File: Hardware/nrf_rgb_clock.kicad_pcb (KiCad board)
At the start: 4 copper layers, 230 x 230 mm, 216 parts, among them J1 Conn_01x02, J3 Conn_01x07_Pin, U2 MP4562, Y1 32MHz

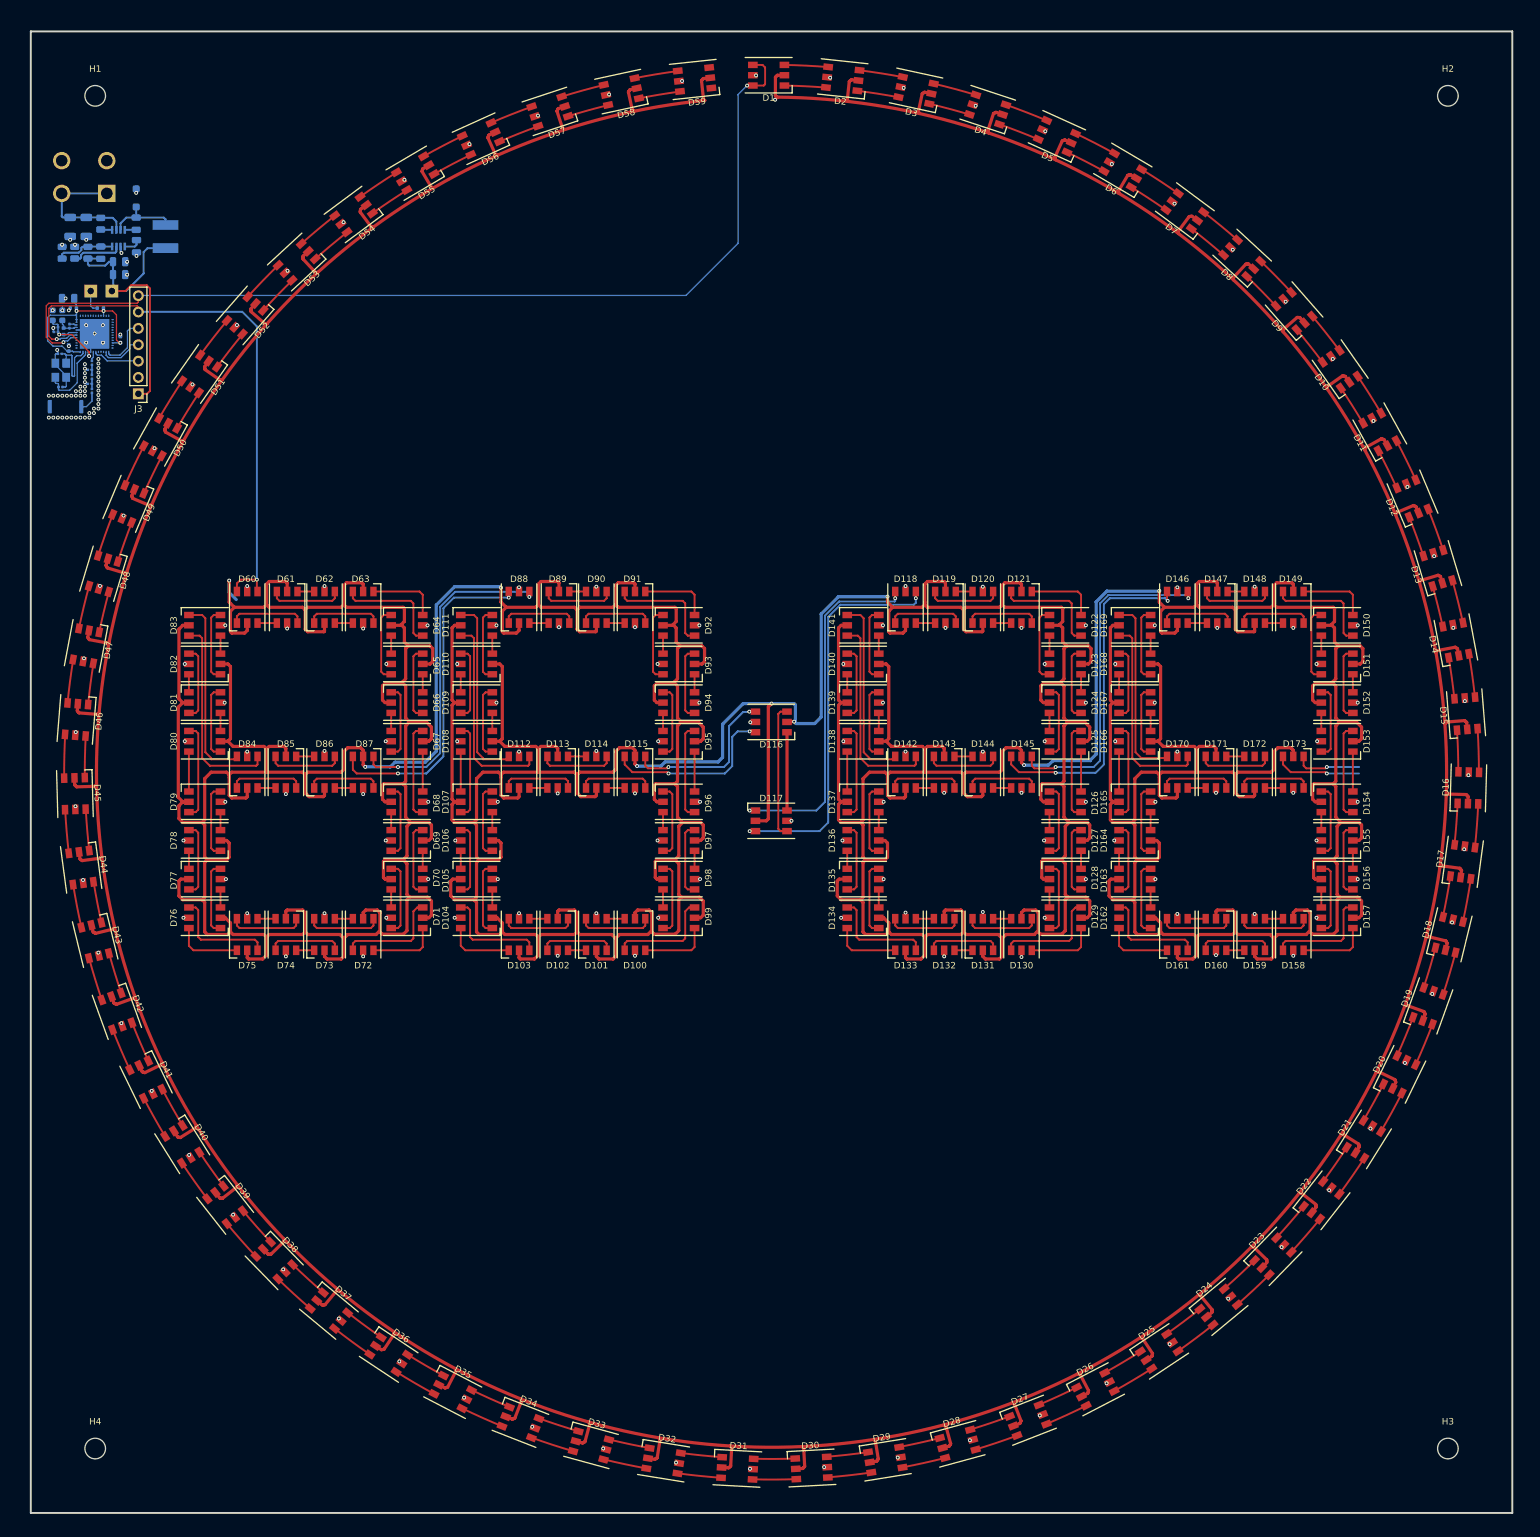
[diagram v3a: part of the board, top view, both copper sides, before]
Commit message: finalized layout, everything on top + LCSC numbers
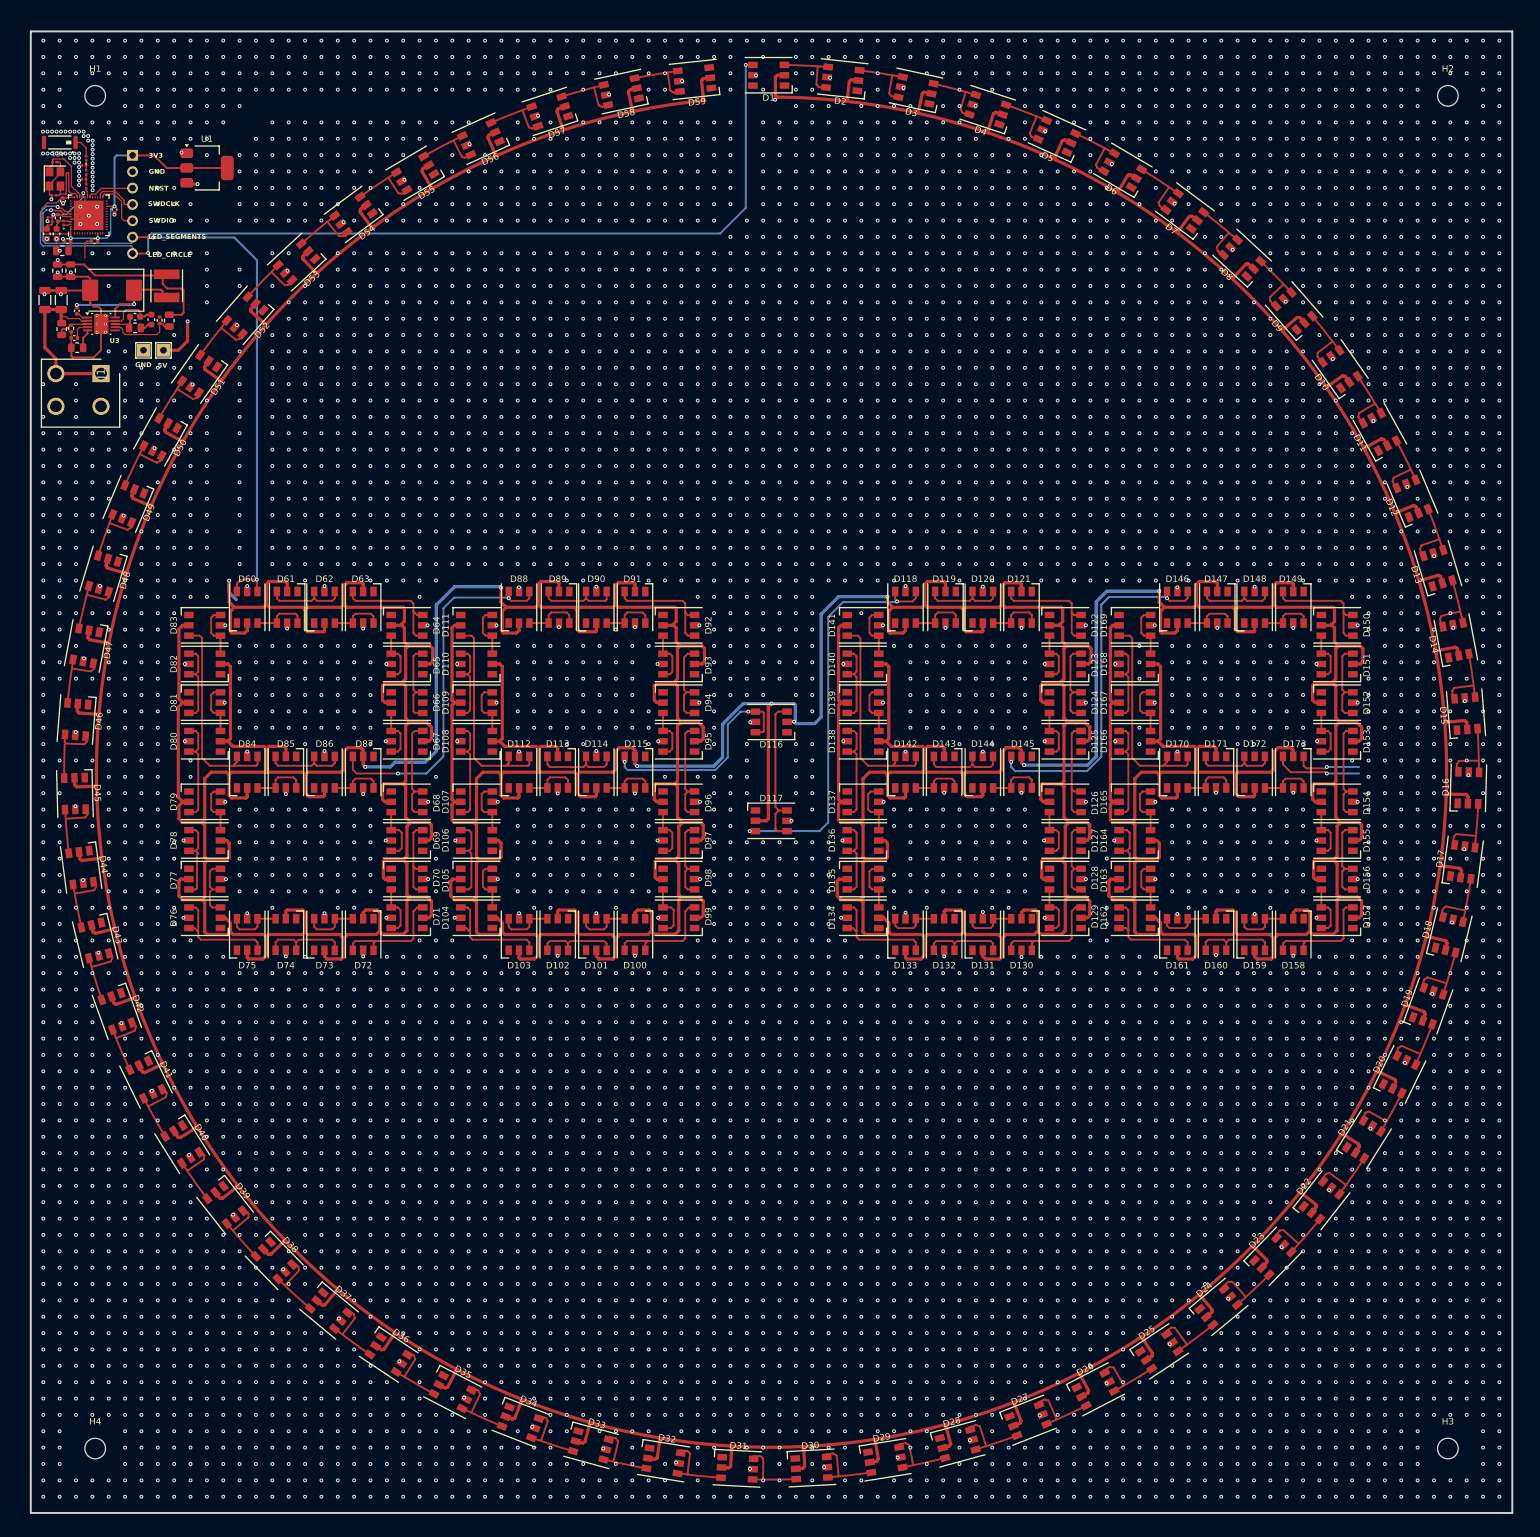
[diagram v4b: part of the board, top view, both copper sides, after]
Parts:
- removed 3V3, GND: TestPoint, TestPoint:TestPoint_THTPad_2.0x2.0mm_Drill1.0mm
- removed C10, C11: 4u7 100VDC, Capacitor_SMD:C_1206_3216Metric
- removed C12: 100n 100VDC, Capacitor_SMD:C_0805_2012Metric
- removed C13, C14: 22u 6.3V, Capacitor_SMD:C_0805_2012Metric
- removed C15: 15p, Capacitor_SMD:C_0805_2012Metric
- removed C16: 22n, Capacitor_SMD:C_0805_2012Metric
- removed D174: ACDBMS2100-HF, Diode_SMD:D_SOD-123F
- removed L5: 10u, ProjectFootprints:NRS5040T3R3NMGJV
- removed R1: 0R, Resistor_SMD:R_0805_2012Metric
- removed R2: 210k, Resistor_SMD:R_0805_2012Metric
- removed R3: 68k, Resistor_SMD:R_0805_2012Metric
- removed R4: 47k, Resistor_SMD:R_0805_2012Metric
- removed U2: MP4562, ProjectFootprints:MP4562
- added C21: 100n, Capacitor_SMD:C_0402_1005Metric, F.Cu at (232.2, 148.6)
- added C22: 47u 6.3V, Capacitor_SMD:C_0805_2012Metric, F.Cu at (229.2, 142.3)
- added C23: 47u 6.3V, Capacitor_SMD:C_0805_2012Metric, F.Cu at (231.2, 142.3)
- added C24: 4u7 100VDC, Capacitor_SMD:C_1206_3216Metric, F.Cu at (227.2, 146.9)
- added C25: 4u7 100VDC, Capacitor_SMD:C_1206_3216Metric, F.Cu at (229.7, 146.9)
- added C26: 10n, Capacitor_SMD:C_0402_1005Metric, F.Cu at (231.8, 152.8)
- added C27: ~, Capacitor_SMD:C_0603_1608Metric, F.Cu at (241.2, 149.5)
- added C28: 4n7, Capacitor_SMD:C_0603_1608Metric, F.Cu at (243.7, 149.9)
- added D175: B360, Diode_SMD:D_SMC, F.Cu at (237.6, 145.4)
- added L6: 10u, ProjectFootprints:NRS5040T3R3NMGJV, F.Cu at (246.1, 144.7)
- added R10: 20k, Resistor_SMD:R_0805_2012Metric, F.Cu at (241.2, 151.2)
- added R11: 27k, Resistor_SMD:R_0805_2012Metric, F.Cu at (246.5, 150.1)
- added R12: 5.1k, Resistor_SMD:R_0402_1005Metric, F.Cu at (245.0, 150.1)
- added R5: 110k, Resistor_SMD:R_0805_2012Metric, F.Cu at (229.8, 151.4)
- added R7: 10k, Resistor_SMD:R_0402_1005Metric, F.Cu at (231.3, 151.3)
- added R9: 412k, Resistor_SMD:R_0805_2012Metric, F.Cu at (232.2, 154.3)
- added TP3: TestPoint, TestPoint:TestPoint_THTPad_2.0x2.0mm_Drill1.0mm, F.Cu at (245.6, 154.7)
- added TP4: TestPoint, TestPoint:TestPoint_THTPad_2.0x2.0mm_Drill1.0mm, F.Cu at (242.5, 154.7)
- added U1: AMS1117-3.3, Package_TO_SOT_SMD:SOT-223-3_TabPin2, F.Cu at (252.3, 126.4)
- added U3: TPS54260DGQ, Package_SO:MSOP-10-1EP_3x3mm_P0.5mm_EP2.2x3.1mm_Mask1.83x1.89mm_ThermalVias, F.Cu at (236.0, 150.6)
- AE1, C1, C17, C18, C19, C2, C20, C3, C4, C5, C6, C7, C8, C9, FB1, J1, L1, L2, L3, L4, U4, Y1: moved to F.Cu
- J3: moved to B.Cu
- moved AE1 41.0 mm to (229.5, 122.4)
- moved J3 37.0 mm to (240.8, 124.4)
- moved L2 36.1 mm to (233.6, 124.9), turned to 90 degrees
- moved C17 34.9 mm to (228.7, 125.5)
- moved C8 33.9 mm to (233.2, 126.0)
- moved L3 31.7 mm to (233.6, 127.1), turned to 90 degrees
- moved Y1 29.7 mm to (228.8, 128.1), turned to -90 degrees
- moved C9 29.6 mm to (233.2, 128.2)
- moved J1 28.0 mm to (235.9, 158.3), turned to -90 degrees
- moved L4 27.4 mm to (233.6, 129.2), turned to 90 degrees
- moved C18 24.6 mm to (228.6, 130.7)
- moved C20 22.8 mm to (230.0, 131.6), turned to 90 degrees
- moved C19 20.2 mm to (238.0, 132.8), turned to 90 degrees
- moved U4 18.4 mm to (234.0, 133.8), turned to 90 degrees
- moved C6 17.8 mm to (228.0, 134.1)
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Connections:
- C1 pad 2: VDD_NRF -> +3V3
- C19 pad 2: VDD_NRF -> +3V3
- C2 pad 2: VDD_NRF -> +3V3
- C20 pad 2: VDD_NRF -> +3V3
- C3 pad 2: VDD_NRF -> +3V3
- D1 pad 1: Net-(D1-BO) -> unconnected-(D1-VCC-Pad1)
- D1 pad 6: LED_CIRCLE -> unconnected-(D1-BI-Pad6)
- D10 pad 1: Net-(D10-BO) -> unconnected-(D10-VCC-Pad1)
- D10 pad 4: Net-(D10-DI) -> Net-(D10-BI)
- D100 pad 1: Net-(D100-BO) -> unconnected-(D100-VCC-Pad1)
- D100 pad 4: Net-(D100-DI) -> Net-(D100-BI)
- D101 pad 1: Net-(D101-BO) -> unconnected-(D101-VCC-Pad1)
- D101 pad 6: Net-(D100-BO) -> Net-(D100-DO)
- D102 pad 1: Net-(D102-BO) -> unconnected-(D102-VCC-Pad1)
- D102 pad 6: Net-(D101-BO) -> Net-(D101-DO)
- D103 pad 1: Net-(D103-BO) -> unconnected-(D103-VCC-Pad1)
- D103 pad 6: Net-(D102-BO) -> Net-(D102-DO)
- D104 pad 1: Net-(D104-BO) -> unconnected-(D104-VCC-Pad1)
- D104 pad 6: Net-(D103-BO) -> Net-(D103-DO)
- D105 pad 1: Net-(D105-BO) -> unconnected-(D105-VCC-Pad1)
- D105 pad 6: Net-(D104-BO) -> Net-(D104-DO)
- D106 pad 1: Net-(D106-BO) -> unconnected-(D106-VCC-Pad1)
- D106 pad 6: Net-(D105-BO) -> Net-(D105-DO)
- D107 pad 1: Net-(D107-BO) -> unconnected-(D107-VCC-Pad1)
- D107 pad 6: Net-(D106-BO) -> Net-(D106-DO)
- D108 pad 1: Net-(D108-BO) -> unconnected-(D108-VCC-Pad1)
- D108 pad 6: Net-(D107-BO) -> Net-(D107-DO)
- D109 pad 1: Net-(D109-BO) -> unconnected-(D109-VCC-Pad1)
- D109 pad 6: Net-(D108-BO) -> Net-(D108-DO)
- D11 pad 1: Net-(D11-BO) -> unconnected-(D11-VCC-Pad1)
- D11 pad 6: Net-(D10-BO) -> Net-(D10-DO)
- D110 pad 1: Net-(D110-BO) -> unconnected-(D110-VCC-Pad1)
- D110 pad 6: Net-(D109-BO) -> Net-(D109-DO)
- D111 pad 1: Net-(D111-BO) -> unconnected-(D111-VCC-Pad1)
- D111 pad 6: Net-(D110-BO) -> Net-(D110-DO)
- D112 pad 1: Net-(D112-BO) -> unconnected-(D112-VCC-Pad1)
- D112 pad 6: Net-(D111-BO) -> Net-(D111-DO)
- D113 pad 1: Net-(D113-BO) -> unconnected-(D113-VCC-Pad1)
- D113 pad 6: Net-(D112-BO) -> Net-(D112-DO)
- D114 pad 1: Net-(D114-BO) -> unconnected-(D114-VCC-Pad1)
- D114 pad 6: Net-(D113-BO) -> Net-(D113-DO)
- D115 pad 1: /led_segment1/LED_BO -> unconnected-(D115-VCC-Pad1)
- D115 pad 6: Net-(D114-BO) -> Net-(D114-DO)
- D116 pad 1: Net-(D116-BO) -> unconnected-(D116-VCC-Pad1)
- D116 pad 4: /led_segment1/LED_BO -> /led_segment1/LED_DO
- D117 pad 1: /led_segment2/LED_BI -> unconnected-(D117-VCC-Pad1)
- D117 pad 6: Net-(D116-BO) -> Net-(D116-DO)
- D118 pad 1: Net-(D118-BO) -> unconnected-(D118-VCC-Pad1)
- D118 pad 6: /led_segment2/LED_BI -> /led_segment2/LED_DI
- D119 pad 1: Net-(D119-BO) -> unconnected-(D119-VCC-Pad1)
- D119 pad 6: Net-(D118-BO) -> Net-(D118-DO)
- D12 pad 1: Net-(D12-BO) -> unconnected-(D12-VCC-Pad1)
- D12 pad 6: Net-(D11-BO) -> Net-(D11-DO)
- D120 pad 1: Net-(D120-BO) -> unconnected-(D120-VCC-Pad1)
- D120 pad 6: Net-(D119-BO) -> Net-(D119-DO)
- D121 pad 1: Net-(D121-BO) -> unconnected-(D121-VCC-Pad1)
- D121 pad 6: Net-(D120-BO) -> Net-(D120-DO)
- D122 pad 1: Net-(D122-BO) -> unconnected-(D122-VCC-Pad1)
- D122 pad 6: Net-(D121-BO) -> Net-(D121-DO)
- D123 pad 1: Net-(D123-BO) -> unconnected-(D123-VCC-Pad1)
- D123 pad 6: Net-(D122-BO) -> Net-(D122-DO)
- D124 pad 1: Net-(D124-BO) -> unconnected-(D124-VCC-Pad1)
- D124 pad 6: Net-(D123-BO) -> Net-(D123-DO)
- D125 pad 1: Net-(D125-BO) -> unconnected-(D125-VCC-Pad1)
- D125 pad 6: Net-(D124-BO) -> Net-(D124-DO)
- D126 pad 1: Net-(D126-BO) -> unconnected-(D126-VCC-Pad1)
- D126 pad 6: Net-(D125-BO) -> Net-(D125-DO)
- D127 pad 1: Net-(D127-BO) -> unconnected-(D127-VCC-Pad1)
- D127 pad 6: Net-(D126-BO) -> Net-(D126-DO)
- D128 pad 1: Net-(D128-BO) -> unconnected-(D128-VCC-Pad1)
- D128 pad 6: Net-(D127-BO) -> Net-(D127-DO)
- D129 pad 1: Net-(D129-BO) -> unconnected-(D129-VCC-Pad1)
- D129 pad 6: Net-(D128-BO) -> Net-(D128-DO)
- D13 pad 1: Net-(D13-BO) -> unconnected-(D13-VCC-Pad1)
- D13 pad 6: Net-(D12-BO) -> Net-(D12-DO)
- D130 pad 1: Net-(D130-BO) -> unconnected-(D130-VCC-Pad1)
- D130 pad 6: Net-(D129-BO) -> Net-(D129-DO)
- D131 pad 1: Net-(D131-BO) -> unconnected-(D131-VCC-Pad1)
- D131 pad 6: Net-(D130-BO) -> Net-(D130-DO)
- D132 pad 1: Net-(D132-BO) -> unconnected-(D132-VCC-Pad1)
- D132 pad 6: Net-(D131-BO) -> Net-(D131-DO)
- D133 pad 1: Net-(D133-BO) -> unconnected-(D133-VCC-Pad1)
- D133 pad 6: Net-(D132-BO) -> Net-(D132-DO)
- D134 pad 1: Net-(D134-BO) -> unconnected-(D134-VCC-Pad1)
- D134 pad 6: Net-(D133-BO) -> Net-(D133-DO)
- D135 pad 1: Net-(D135-BO) -> unconnected-(D135-VCC-Pad1)
- D135 pad 6: Net-(D134-BO) -> Net-(D134-DO)
- D136 pad 1: Net-(D136-BO) -> unconnected-(D136-VCC-Pad1)
- D136 pad 6: Net-(D135-BO) -> Net-(D135-DO)
- D137 pad 1: Net-(D137-BO) -> unconnected-(D137-VCC-Pad1)
- D137 pad 6: Net-(D136-BO) -> Net-(D136-DO)
- D138 pad 1: Net-(D138-BO) -> unconnected-(D138-VCC-Pad1)
- D138 pad 6: Net-(D137-BO) -> Net-(D137-DO)
- D139 pad 1: Net-(D139-BO) -> unconnected-(D139-VCC-Pad1)
- D139 pad 6: Net-(D138-BO) -> Net-(D138-DO)
- D14 pad 1: Net-(D14-BO) -> unconnected-(D14-VCC-Pad1)
- D14 pad 6: Net-(D13-BO) -> Net-(D13-DO)
- D140 pad 1: Net-(D140-BO) -> unconnected-(D140-VCC-Pad1)
- D140 pad 6: Net-(D139-BO) -> Net-(D139-DO)
- D141 pad 1: Net-(D141-BO) -> unconnected-(D141-VCC-Pad1)
- D141 pad 6: Net-(D140-BO) -> Net-(D140-DO)
- D142 pad 1: Net-(D142-BO) -> unconnected-(D142-VCC-Pad1)
- D142 pad 6: Net-(D141-BO) -> Net-(D141-DO)
- D143 pad 1: Net-(D143-BO) -> unconnected-(D143-VCC-Pad1)
- D143 pad 6: Net-(D142-BO) -> Net-(D142-DO)
- D144 pad 1: Net-(D144-BO) -> unconnected-(D144-VCC-Pad1)
- D144 pad 6: Net-(D143-BO) -> Net-(D143-DO)
- D145 pad 1: /led_segment2/LED_BO -> unconnected-(D145-VCC-Pad1)
- D145 pad 6: Net-(D144-BO) -> Net-(D144-DO)
- D146 pad 1: Net-(D146-BO) -> unconnected-(D146-VCC-Pad1)
- D146 pad 4: /led_segment2/LED_BO -> /led_segment2/LED_DO
- D147 pad 1: Net-(D147-BO) -> unconnected-(D147-VCC-Pad1)
- D147 pad 6: Net-(D146-BO) -> Net-(D146-DO)
- D148 pad 1: Net-(D148-BO) -> unconnected-(D148-VCC-Pad1)
- D148 pad 6: Net-(D147-BO) -> Net-(D147-DO)
- D149 pad 1: Net-(D149-BO) -> unconnected-(D149-VCC-Pad1)
- D149 pad 6: Net-(D148-BO) -> Net-(D148-DO)
- D15 pad 1: Net-(D15-BO) -> unconnected-(D15-VCC-Pad1)
- D15 pad 6: Net-(D14-BO) -> Net-(D14-DO)
- D150 pad 1: Net-(D150-BO) -> unconnected-(D150-VCC-Pad1)
- D150 pad 6: Net-(D149-BO) -> Net-(D149-DO)
- D151 pad 1: Net-(D151-BO) -> unconnected-(D151-VCC-Pad1)
- D151 pad 6: Net-(D150-BO) -> Net-(D150-DO)
- D152 pad 1: Net-(D152-BO) -> unconnected-(D152-VCC-Pad1)
- D152 pad 6: Net-(D151-BO) -> Net-(D151-DO)
- D153 pad 1: Net-(D153-BO) -> unconnected-(D153-VCC-Pad1)
- D153 pad 6: Net-(D152-BO) -> Net-(D152-DO)
- D154 pad 1: Net-(D154-BO) -> unconnected-(D154-VCC-Pad1)
- D154 pad 6: Net-(D153-BO) -> Net-(D153-DO)
- D155 pad 1: Net-(D155-BO) -> unconnected-(D155-VCC-Pad1)
- D155 pad 6: Net-(D154-BO) -> Net-(D154-DO)
- D156 pad 1: Net-(D156-BO) -> unconnected-(D156-VCC-Pad1)
- D156 pad 6: Net-(D155-BO) -> Net-(D155-DO)
- D157 pad 1: Net-(D157-BO) -> unconnected-(D157-VCC-Pad1)
- D157 pad 6: Net-(D156-BO) -> Net-(D156-DO)
- D158 pad 1: Net-(D158-BO) -> unconnected-(D158-VCC-Pad1)
- D158 pad 6: Net-(D157-BO) -> Net-(D157-DO)
- D159 pad 1: Net-(D159-BO) -> unconnected-(D159-VCC-Pad1)
- D159 pad 6: Net-(D158-BO) -> Net-(D158-DO)
- D16 pad 1: Net-(D16-BO) -> unconnected-(D16-VCC-Pad1)
- D16 pad 6: Net-(D15-BO) -> Net-(D15-DO)
- D160 pad 1: Net-(D160-BO) -> unconnected-(D160-VCC-Pad1)
- D160 pad 6: Net-(D159-BO) -> Net-(D159-DO)
- D161 pad 1: Net-(D161-BO) -> unconnected-(D161-VCC-Pad1)
- D161 pad 6: Net-(D160-BO) -> Net-(D160-DO)
- D162 pad 1: Net-(D162-BO) -> unconnected-(D162-VCC-Pad1)
- D162 pad 6: Net-(D161-BO) -> Net-(D161-DO)
- D163 pad 1: Net-(D163-BO) -> unconnected-(D163-VCC-Pad1)
- D163 pad 6: Net-(D162-BO) -> Net-(D162-DO)
- D164 pad 1: Net-(D164-BO) -> unconnected-(D164-VCC-Pad1)
- D164 pad 6: Net-(D163-BO) -> Net-(D163-DO)
- D165 pad 1: Net-(D165-BO) -> unconnected-(D165-VCC-Pad1)
- D165 pad 6: Net-(D164-BO) -> Net-(D164-DO)
- D166 pad 1: Net-(D166-BO) -> unconnected-(D166-VCC-Pad1)
- D166 pad 6: Net-(D165-BO) -> Net-(D165-DO)
- D167 pad 1: Net-(D167-BO) -> unconnected-(D167-VCC-Pad1)
- D167 pad 6: Net-(D166-BO) -> Net-(D166-DO)
- D168 pad 1: Net-(D168-BO) -> unconnected-(D168-VCC-Pad1)
- D168 pad 6: Net-(D167-BO) -> Net-(D167-DO)
- D169 pad 1: Net-(D169-BO) -> unconnected-(D169-VCC-Pad1)
- D169 pad 6: Net-(D168-BO) -> Net-(D168-DO)
- D17 pad 1: Net-(D17-BO) -> unconnected-(D17-VCC-Pad1)
- D17 pad 6: Net-(D16-BO) -> Net-(D16-DO)
- D170 pad 1: Net-(D170-BO) -> unconnected-(D170-VCC-Pad1)
- D170 pad 6: Net-(D169-BO) -> Net-(D169-DO)
- D171 pad 1: Net-(D171-BO) -> unconnected-(D171-VCC-Pad1)
- D171 pad 6: Net-(D170-BO) -> Net-(D170-DO)
- D172 pad 1: Net-(D172-BO) -> unconnected-(D172-VCC-Pad1)
- D172 pad 6: Net-(D171-BO) -> Net-(D171-DO)
- D173 pad 1: /led_segment3/LED_BO -> unconnected-(D173-VCC-Pad1)
- D173 pad 6: Net-(D172-BO) -> Net-(D172-DO)
- D18 pad 1: Net-(D18-BO) -> unconnected-(D18-VCC-Pad1)
- D18 pad 6: Net-(D17-BO) -> Net-(D17-DO)
- D19 pad 1: Net-(D19-BO) -> unconnected-(D19-VCC-Pad1)
- D19 pad 6: Net-(D18-BO) -> Net-(D18-DO)
- D2 pad 1: Net-(D2-BO) -> unconnected-(D2-VCC-Pad1)
- D2 pad 6: Net-(D1-BO) -> Net-(D1-DO)
- D20 pad 1: Net-(D20-BO) -> unconnected-(D20-VCC-Pad1)
- D20 pad 6: Net-(D19-BO) -> Net-(D19-DO)
- D21 pad 1: Net-(D21-BO) -> unconnected-(D21-VCC-Pad1)
- D21 pad 6: Net-(D20-BO) -> Net-(D20-DO)
- D22 pad 1: Net-(D22-BO) -> unconnected-(D22-VCC-Pad1)
- D22 pad 6: Net-(D21-BO) -> Net-(D21-DO)
- D23 pad 1: Net-(D23-BO) -> unconnected-(D23-VCC-Pad1)
- D23 pad 6: Net-(D22-BO) -> Net-(D22-DO)
- D24 pad 1: Net-(D24-BO) -> unconnected-(D24-VCC-Pad1)
- D24 pad 6: Net-(D23-BO) -> Net-(D23-DO)
- D25 pad 1: Net-(D25-BO) -> unconnected-(D25-VCC-Pad1)
- D25 pad 6: Net-(D24-BO) -> Net-(D24-DO)
- D26 pad 1: Net-(D26-BO) -> unconnected-(D26-VCC-Pad1)
- D26 pad 6: Net-(D25-BO) -> Net-(D25-DO)
- D27 pad 1: Net-(D27-BO) -> unconnected-(D27-VCC-Pad1)
- D27 pad 6: Net-(D26-BO) -> Net-(D26-DO)
- D28 pad 1: Net-(D28-BO) -> unconnected-(D28-VCC-Pad1)
- D28 pad 6: Net-(D27-BO) -> Net-(D27-DO)
- D29 pad 1: Net-(D29-BO) -> unconnected-(D29-VCC-Pad1)
- D29 pad 6: Net-(D28-BO) -> Net-(D28-DO)
- D3 pad 1: Net-(D3-BO) -> unconnected-(D3-VCC-Pad1)
- D3 pad 6: Net-(D2-BO) -> Net-(D2-DO)
- D30 pad 1: Net-(D30-BO) -> unconnected-(D30-VCC-Pad1)
- D30 pad 6: Net-(D29-BO) -> Net-(D29-DO)
- D31 pad 1: Net-(D31-BO) -> unconnected-(D31-VCC-Pad1)
- D31 pad 6: Net-(D30-BO) -> Net-(D30-DO)
- D32 pad 1: Net-(D32-BO) -> unconnected-(D32-VCC-Pad1)
- D32 pad 6: Net-(D31-BO) -> Net-(D31-DO)
- D33 pad 1: Net-(D33-BO) -> unconnected-(D33-VCC-Pad1)
- D33 pad 6: Net-(D32-BO) -> Net-(D32-DO)
- D34 pad 1: Net-(D34-BO) -> unconnected-(D34-VCC-Pad1)
- D34 pad 6: Net-(D33-BO) -> Net-(D33-DO)
- D35 pad 1: Net-(D35-BO) -> unconnected-(D35-VCC-Pad1)
- D35 pad 6: Net-(D34-BO) -> Net-(D34-DO)
- D36 pad 1: Net-(D36-BO) -> unconnected-(D36-VCC-Pad1)
- D36 pad 6: Net-(D35-BO) -> Net-(D35-DO)
- D37 pad 1: Net-(D37-BO) -> unconnected-(D37-VCC-Pad1)
- D37 pad 6: Net-(D36-BO) -> Net-(D36-DO)
- D38 pad 1: Net-(D38-BO) -> unconnected-(D38-VCC-Pad1)
- D38 pad 6: Net-(D37-BO) -> Net-(D37-DO)
- D39 pad 1: Net-(D39-BO) -> unconnected-(D39-VCC-Pad1)
- D39 pad 6: Net-(D38-BO) -> Net-(D38-DO)
- D4 pad 1: Net-(D4-BO) -> unconnected-(D4-VCC-Pad1)
- D4 pad 6: Net-(D3-BO) -> Net-(D3-DO)
- D40 pad 1: Net-(D40-BO) -> unconnected-(D40-VCC-Pad1)
- D40 pad 6: Net-(D39-BO) -> Net-(D39-DO)
- D41 pad 1: Net-(D41-BO) -> unconnected-(D41-VCC-Pad1)
- D41 pad 6: Net-(D40-BO) -> Net-(D40-DO)
- D42 pad 1: Net-(D42-BO) -> unconnected-(D42-VCC-Pad1)
- D42 pad 6: Net-(D41-BO) -> Net-(D41-DO)
- D43 pad 1: Net-(D43-BO) -> unconnected-(D43-VCC-Pad1)
- D43 pad 6: Net-(D42-BO) -> Net-(D42-DO)
- D44 pad 1: Net-(D44-BO) -> unconnected-(D44-VCC-Pad1)
- D44 pad 6: Net-(D43-BO) -> Net-(D43-DO)
- D45 pad 1: Net-(D45-BO) -> unconnected-(D45-VCC-Pad1)
- D45 pad 6: Net-(D44-BO) -> Net-(D44-DO)
- D46 pad 1: Net-(D46-BO) -> unconnected-(D46-VCC-Pad1)
- D46 pad 6: Net-(D45-BO) -> Net-(D45-DO)
- D47 pad 1: Net-(D47-BO) -> unconnected-(D47-VCC-Pad1)
- D47 pad 6: Net-(D46-BO) -> Net-(D46-DO)
- D48 pad 1: Net-(D48-BO) -> unconnected-(D48-VCC-Pad1)
- D48 pad 6: Net-(D47-BO) -> Net-(D47-DO)
- D49 pad 1: Net-(D49-BO) -> unconnected-(D49-VCC-Pad1)
- D49 pad 6: Net-(D48-BO) -> Net-(D48-DO)
- D5 pad 1: Net-(D5-BO) -> unconnected-(D5-VCC-Pad1)
- D5 pad 6: Net-(D4-BO) -> Net-(D4-DO)
- D50 pad 1: Net-(D50-BO) -> unconnected-(D50-VCC-Pad1)
- D50 pad 6: Net-(D49-BO) -> Net-(D49-DO)
- D51 pad 1: Net-(D51-BO) -> unconnected-(D51-VCC-Pad1)
- D51 pad 6: Net-(D50-BO) -> Net-(D50-DO)
- D52 pad 1: Net-(D52-BO) -> unconnected-(D52-VCC-Pad1)
- D52 pad 6: Net-(D51-BO) -> Net-(D51-DO)
- D53 pad 1: Net-(D53-BO) -> unconnected-(D53-VCC-Pad1)
- D53 pad 6: Net-(D52-BO) -> Net-(D52-DO)
- D54 pad 1: Net-(D54-BO) -> unconnected-(D54-VCC-Pad1)
- D54 pad 6: Net-(D53-BO) -> Net-(D53-DO)
- D55 pad 1: Net-(D55-BO) -> unconnected-(D55-VCC-Pad1)
- D55 pad 6: Net-(D54-BO) -> Net-(D54-DO)
- D56 pad 1: Net-(D56-BO) -> unconnected-(D56-VCC-Pad1)
- D56 pad 6: Net-(D55-BO) -> Net-(D55-DO)
- D57 pad 1: Net-(D57-BO) -> unconnected-(D57-VCC-Pad1)
- D57 pad 6: Net-(D56-BO) -> Net-(D56-DO)
- D58 pad 1: Net-(D58-BO) -> unconnected-(D58-VCC-Pad1)
- D58 pad 6: Net-(D57-BO) -> Net-(D57-DO)
- D59 pad 6: Net-(D58-BO) -> Net-(D58-DO)
- D6 pad 1: Net-(D6-BO) -> unconnected-(D6-VCC-Pad1)
- D6 pad 6: Net-(D5-BO) -> Net-(D5-DO)
- D60 pad 1: Net-(D60-BO) -> unconnected-(D60-VCC-Pad1)
- D61 pad 1: Net-(D61-BO) -> unconnected-(D61-VCC-Pad1)
- D61 pad 6: Net-(D60-BO) -> Net-(D60-DO)
- D62 pad 1: Net-(D62-BO) -> unconnected-(D62-VCC-Pad1)
- D62 pad 6: Net-(D61-BO) -> Net-(D61-DO)
- D63 pad 1: Net-(D63-BO) -> unconnected-(D63-VCC-Pad1)
- D63 pad 6: Net-(D62-BO) -> Net-(D62-DO)
- D64 pad 1: Net-(D64-BO) -> unconnected-(D64-VCC-Pad1)
- D64 pad 6: Net-(D63-BO) -> Net-(D63-DO)
- D65 pad 1: Net-(D65-BO) -> unconnected-(D65-VCC-Pad1)
- D65 pad 6: Net-(D64-BO) -> Net-(D64-DO)
- D66 pad 1: Net-(D66-BO) -> unconnected-(D66-VCC-Pad1)
- D66 pad 6: Net-(D65-BO) -> Net-(D65-DO)
- D67 pad 1: Net-(D67-BO) -> unconnected-(D67-VCC-Pad1)
- D67 pad 6: Net-(D66-BO) -> Net-(D66-DO)
- D68 pad 1: Net-(D68-BO) -> unconnected-(D68-VCC-Pad1)
- D68 pad 6: Net-(D67-BO) -> Net-(D67-DO)
- D69 pad 1: Net-(D69-BO) -> unconnected-(D69-VCC-Pad1)
- D69 pad 6: Net-(D68-BO) -> Net-(D68-DO)
- D7 pad 1: Net-(D7-BO) -> unconnected-(D7-VCC-Pad1)
- D7 pad 6: Net-(D6-BO) -> Net-(D6-DO)
- D70 pad 1: Net-(D70-BO) -> unconnected-(D70-VCC-Pad1)
- D70 pad 6: Net-(D69-BO) -> Net-(D69-DO)
- D71 pad 1: Net-(D71-BO) -> unconnected-(D71-VCC-Pad1)
- D71 pad 6: Net-(D70-BO) -> Net-(D70-DO)
- D72 pad 1: Net-(D72-BO) -> unconnected-(D72-VCC-Pad1)
- D72 pad 6: Net-(D71-BO) -> Net-(D71-DO)
- D73 pad 1: Net-(D73-BO) -> unconnected-(D73-VCC-Pad1)
- D73 pad 6: Net-(D72-BO) -> Net-(D72-DO)
- D74 pad 1: Net-(D74-BO) -> unconnected-(D74-VCC-Pad1)
- D74 pad 6: Net-(D73-BO) -> Net-(D73-DO)
- D75 pad 1: Net-(D75-BO) -> unconnected-(D75-VCC-Pad1)
- D75 pad 6: Net-(D74-BO) -> Net-(D74-DO)
- D76 pad 1: Net-(D76-BO) -> unconnected-(D76-VCC-Pad1)
- D76 pad 6: Net-(D75-BO) -> Net-(D75-DO)
- D77 pad 1: Net-(D77-BO) -> unconnected-(D77-VCC-Pad1)
- D77 pad 6: Net-(D76-BO) -> Net-(D76-DO)
- D78 pad 1: Net-(D78-BO) -> unconnected-(D78-VCC-Pad1)
- D78 pad 6: Net-(D77-BO) -> Net-(D77-DO)
- D79 pad 1: Net-(D79-BO) -> unconnected-(D79-VCC-Pad1)
- D79 pad 6: Net-(D78-BO) -> Net-(D78-DO)
- D8 pad 1: Net-(D8-BO) -> unconnected-(D8-VCC-Pad1)
- D8 pad 6: Net-(D7-BO) -> Net-(D7-DO)
- D80 pad 1: Net-(D80-BO) -> unconnected-(D80-VCC-Pad1)
- D80 pad 6: Net-(D79-BO) -> Net-(D79-DO)
- D81 pad 1: Net-(D81-BO) -> unconnected-(D81-VCC-Pad1)
- D81 pad 6: Net-(D80-BO) -> Net-(D80-DO)
- D82 pad 1: Net-(D82-BO) -> unconnected-(D82-VCC-Pad1)
- D82 pad 6: Net-(D81-BO) -> Net-(D81-DO)
- D83 pad 1: Net-(D83-BO) -> unconnected-(D83-VCC-Pad1)
- D83 pad 6: Net-(D82-BO) -> Net-(D82-DO)
- D84 pad 1: Net-(D84-BO) -> unconnected-(D84-VCC-Pad1)
- D84 pad 6: Net-(D83-BO) -> Net-(D83-DO)
- D85 pad 1: Net-(D85-BO) -> unconnected-(D85-VCC-Pad1)
- D85 pad 6: Net-(D84-BO) -> Net-(D84-DO)
- D86 pad 1: Net-(D86-BO) -> unconnected-(D86-VCC-Pad1)
- D86 pad 6: Net-(D85-BO) -> Net-(D85-DO)
- D87 pad 1: /led_segment/LED_BO -> unconnected-(D87-VCC-Pad1)
- D87 pad 6: Net-(D86-BO) -> Net-(D86-DO)
- D88 pad 1: Net-(D88-BO) -> unconnected-(D88-VCC-Pad1)
- D88 pad 4: /led_segment/LED_BO -> /led_segment/LED_DO
- D89 pad 1: Net-(D89-BO) -> unconnected-(D89-VCC-Pad1)
- D89 pad 6: Net-(D88-BO) -> Net-(D88-DO)
- D9 pad 1: Net-(D10-BI) -> unconnected-(D9-VCC-Pad1)
- D9 pad 3: Net-(D10-DI) -> Net-(D10-BI)
- D9 pad 6: Net-(D8-BO) -> Net-(D8-DO)
- D90 pad 1: Net-(D90-BO) -> unconnected-(D90-VCC-Pad1)
- D90 pad 6: Net-(D89-BO) -> Net-(D89-DO)
- D91 pad 1: Net-(D91-BO) -> unconnected-(D91-VCC-Pad1)
- D91 pad 6: Net-(D90-BO) -> Net-(D90-DO)
- D92 pad 1: Net-(D92-BO) -> unconnected-(D92-VCC-Pad1)
- D92 pad 6: Net-(D91-BO) -> Net-(D91-DO)
- D93 pad 1: Net-(D93-BO) -> unconnected-(D93-VCC-Pad1)
- D93 pad 6: Net-(D92-BO) -> Net-(D92-DO)
- D94 pad 1: Net-(D94-BO) -> unconnected-(D94-VCC-Pad1)
- D94 pad 6: Net-(D93-BO) -> Net-(D93-DO)
- D95 pad 1: Net-(D95-BO) -> unconnected-(D95-VCC-Pad1)
- D95 pad 6: Net-(D94-BO) -> Net-(D94-DO)
- D96 pad 1: Net-(D96-BO) -> unconnected-(D96-VCC-Pad1)
- D96 pad 6: Net-(D95-BO) -> Net-(D95-DO)
- D97 pad 1: Net-(D97-BO) -> unconnected-(D97-VCC-Pad1)
- D97 pad 6: Net-(D96-BO) -> Net-(D96-DO)
- D98 pad 1: Net-(D98-BO) -> unconnected-(D98-VCC-Pad1)
- D98 pad 6: Net-(D97-BO) -> Net-(D97-DO)
- D99 pad 1: Net-(D100-BI) -> unconnected-(D99-VCC-Pad1)
- D99 pad 3: Net-(D100-DI) -> Net-(D100-BI)
- D99 pad 6: Net-(D98-BO) -> Net-(D98-DO)
- U4 pad 10: VDD_NRF -> +3V3
- U4 pad 22: VDD_NRF -> +3V3
- U4 pad 36: VDD_NRF -> +3V3
- U4 pad 47: VDD_NRF -> +3V3
- U4 pad 48: VDD_NRF -> +3V3
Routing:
- net +5V: track 2003.1 -> 2251.0 mm, vias 10 -> 13
- net /led_segment2/LED_BI: track 55.4 -> 0.00 mm, vias 2 -> 0
- net /led_segment2/LED_BO: track 52.8 -> 0.00 mm, vias 2 -> 0
- net /led_segment/LED_BO: track 51.7 -> 0.00 mm, vias 2 -> 0
- net GND: track 111.7 -> 156.4 mm, vias 236 -> 6560
- net VDD_NRF: track 31.9 -> 0.00 mm, vias 3 -> 0
- net Net-(D141-BO): track 29.2 -> 0.00 mm
- net Net-(D111-BO): track 29.2 -> 0.00 mm
- net Net-(D83-BO): track 29.2 -> 0.00 mm
- net Net-(D169-BO): track 28.9 -> 0.00 mm
- net /led_segment1/LED_BO: track 25.6 -> 0.00 mm, vias 2 -> 0
- net Net-(D175-K): track 0.00 -> 22.0 mm, vias 0 -> 2
- net Net-(D100-DI): track 16.7 -> 0.00 mm
- net Net-(D116-BO): track 12.2 -> 0.00 mm
- net Net-(D146-BO): track 11.8 -> 0.00 mm
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- added copper zone on In2.Cu, net GND
- removed copper zone on In2.Cu, net +5V
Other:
- board text added: "5V"
